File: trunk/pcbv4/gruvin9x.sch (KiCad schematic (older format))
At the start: 215 parts, among them IC1 ATMEGA2560-A_GRUVIN, J4 JUMPER_2W, K1 CONN_3, K2 CONN_3, K3 CONN_3, K4 CONN_3, P1 CONN_3X2, P10 CONN_5X2, P11 CONN_1, P12 CONN_4, P13 CONN_8, P14 CONN_2, P15 CONN_4, P16 CONN_1, P17 CONN_1, P18 CONN_2, P19 CONN_8, P2 CONN_5, P20 CONN_8, P21 CONN_4, P22 CONN_1, P23 CONN_1, P24 CONN_1, P3 CONN_6, P4 CONN_9, P5 CONN_9, P6 CONN_6, P7 CONN_12, P8 CONN_30_LCD_GRUVIN, P9 CONN_1, Q1 BC847C, Q2 BC847C, Q3 BC857C, Q4 BC847C, Q5 BC847C, Q7 BC847C, SW1 SW_PUSH, SW2 SW_PUSH, SW3 SW_PUSH, SW4 SW_PUSH, SW5 SW_PUSH, SW6 SW_PUSH, U1 78L05, U3 LN-6206-30, U4 TPS77601, X1 16MHz 18pf

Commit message: Copper pour additions to V4 and silkscreen update. Also moved silkscreen labels so no text exists over pads.
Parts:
- added P25, P26: CONN_1, symbol CONN_1
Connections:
- wire segments 641 -> 645

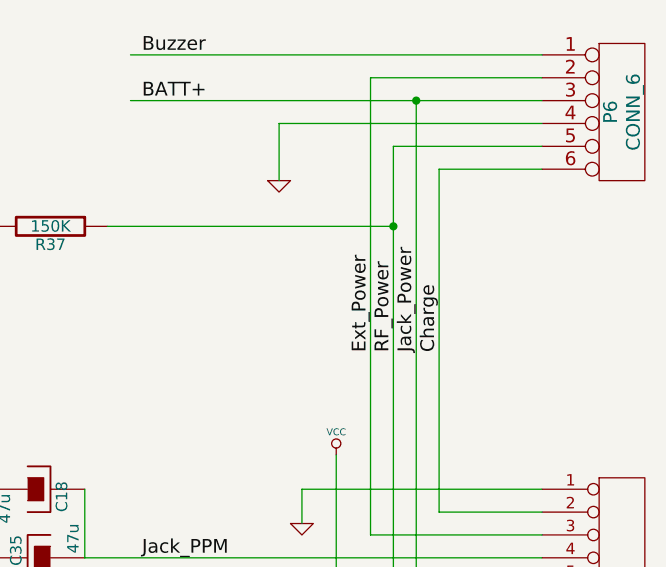
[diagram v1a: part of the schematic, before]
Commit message: Correction to label on schematic, only a cosmetic error
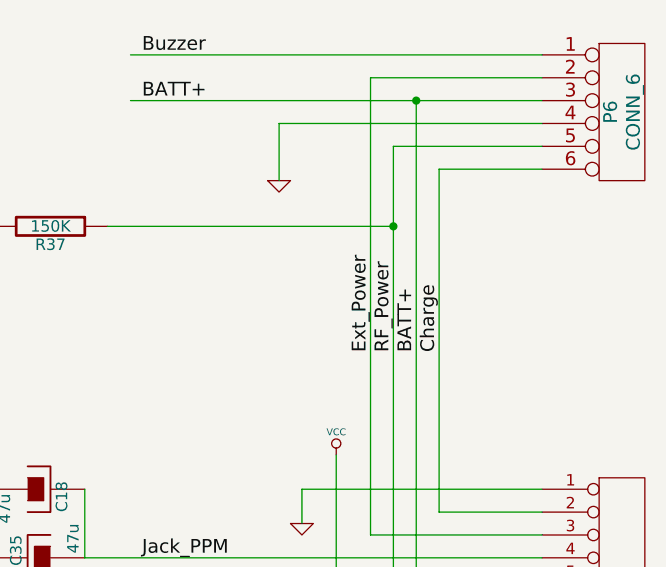
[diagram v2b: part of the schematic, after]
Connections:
- net labels removed: Jack_Power
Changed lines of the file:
@@
-EESchema Schematic File Version 2  date 29/06/2011 00:35:47
+EESchema Schematic File Version 2  date 30/06/2011 00:19:45
 LIBS:device
 LIBS:transistors
@@
 Sheet 1 1
 Title "Main Controller PCB for 100pin ATMega"
-Date "28 jun 2011"
+Date "29 jun 2011"
 Rev "4.0"
 Comp ""
@@
 RF_Power
 Text Label 18550 9950 1    60   ~ 0
-Jack_Power
+BATT+
 $Comp
 L GND #PWR70

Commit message: 1st BOM for V4. Also includes part references for Farnell UK. Still need to find alternatives for the regulators. Also added units to some to the components in the schematic that had none.
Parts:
- C1, C11: value 10u -> 10uF
- C10, C15, C17, C19, C2, C20, C21, C22, C23, C24, C25, C26, C27, C28, C29, C3, C30, C33, C34, C36, C4, C5, C6, C7, C8, C9, C91, C92, C93, C94, C95, C96: value 0.1 -> 0.1uF
- C12, C18, C31, C35: value 47u -> 47uF
- C13, C14: value 18p -> 18pF
- C16, C44, C45, C46, C47, C48, C49, C50, C51, C52: value 1u -> 1uF
- C32: value 22u -> 22uF
- D1: value DIODE -> DIODESIL
- L1, L2: value 10u -> 10uH
- R10, R11, R12, R13, R14, R18, R19, R20, R21, R22, R26, R3, R4, R5, R6, R68, R70, R71, R8, R83, R84, R9: value 200 -> 200R
- R15: value 110K -> 100K
- R39, R40, R78: value 0 -> 0R
- R7: value 332K -> 180K
- R91, R92, R93, R94, R95, R96: value 220R -> 200R
- X1: value 16MHz 18pf -> 16MHz
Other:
- note added: "R7/R15 Combo gives 3.11v"

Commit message: Added yet another breakout header for driving the Hobbyking LED backlight kit via the Spare1 signal. Also updated BOM to include rotary encoders.
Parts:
- added P27: CONN_2, CONN_2MM_2x1, symbol CONN_2
- added Q6: BC847C, SOT23-BCE, symbol BC847C
- added R85: 5K1, symbol R
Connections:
- wire segments 645 -> 651
